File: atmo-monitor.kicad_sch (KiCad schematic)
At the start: 29 parts, among them J1 E-Ink, J3 Qwiic, J4 PM Sensor, Q1 IRLML0100TRPbF, SW1 Reset, SW2 1825232-1, U1 STM32F103CBT6, U2 LP2950-3.3_TO252, U3 Power

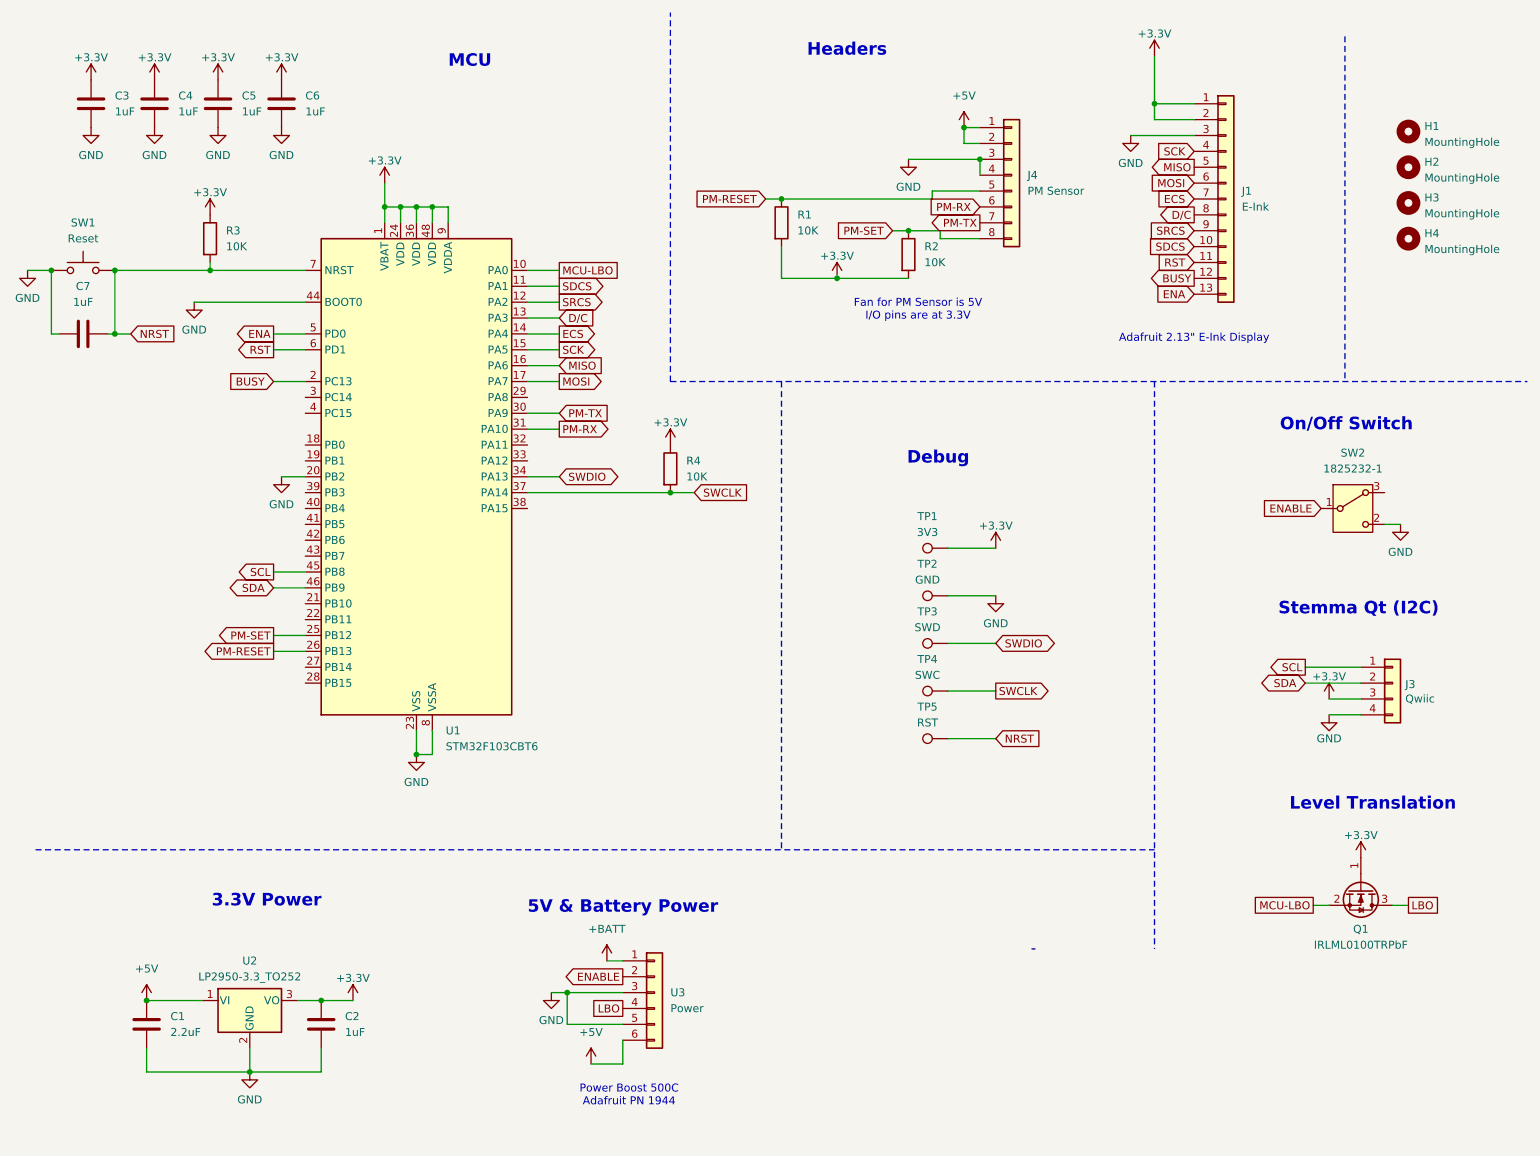
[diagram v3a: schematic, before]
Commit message: Added R5 for LBO pull up on MCU
For proper level translation, need R5
Swapped RX and TX on PMS jumper so that it is legibly correct
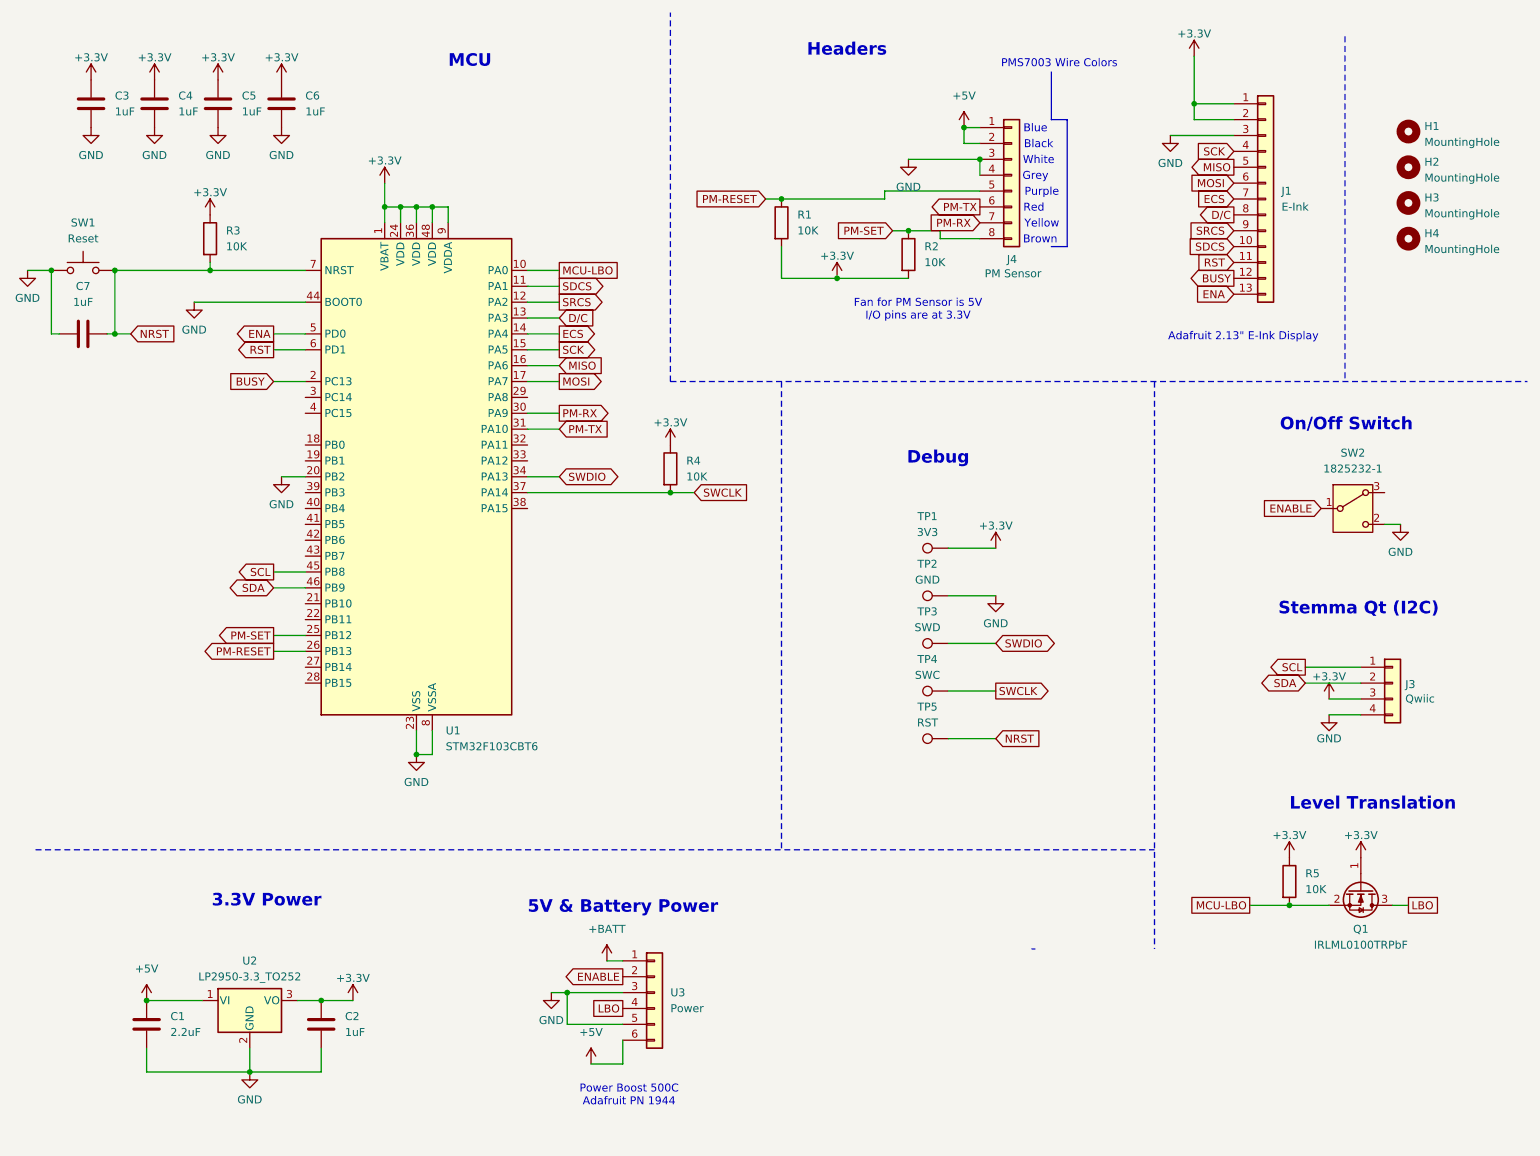
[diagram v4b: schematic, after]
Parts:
- added R5: 10K, Resistor_SMD:R_1206_3216Metric_Pad1.30x1.75mm_HandSolder, symbol Device:R
- SW1: footprint (none) -> custom_footprint:OnShine KPT-1187B
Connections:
- net +3.3V: now also R5.1
- net MCU-LBO: now also R5.2
- net PM-RX: now also J4.7 (Pin_7), U1.30 (PA9); no longer J4.6 (Pin_6), U1.31 (PA10)
- net PM-TX: now also J4.6 (Pin_6), U1.31 (PA10); no longer J4.7 (Pin_7), U1.30 (PA9)
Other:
- note added: "Black"
- note added: "Blue"
- note added: "Brown"
- note added: "Grey"
- note added: "PMS7003 Wire Colors"
- note added: "Purple"
- note added: "Red"
- note added: "White"
- note added: "Yellow"
- moved on the sheet: J1

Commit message: Finished schematic drc checks
Update pdb from schematic, no real changes
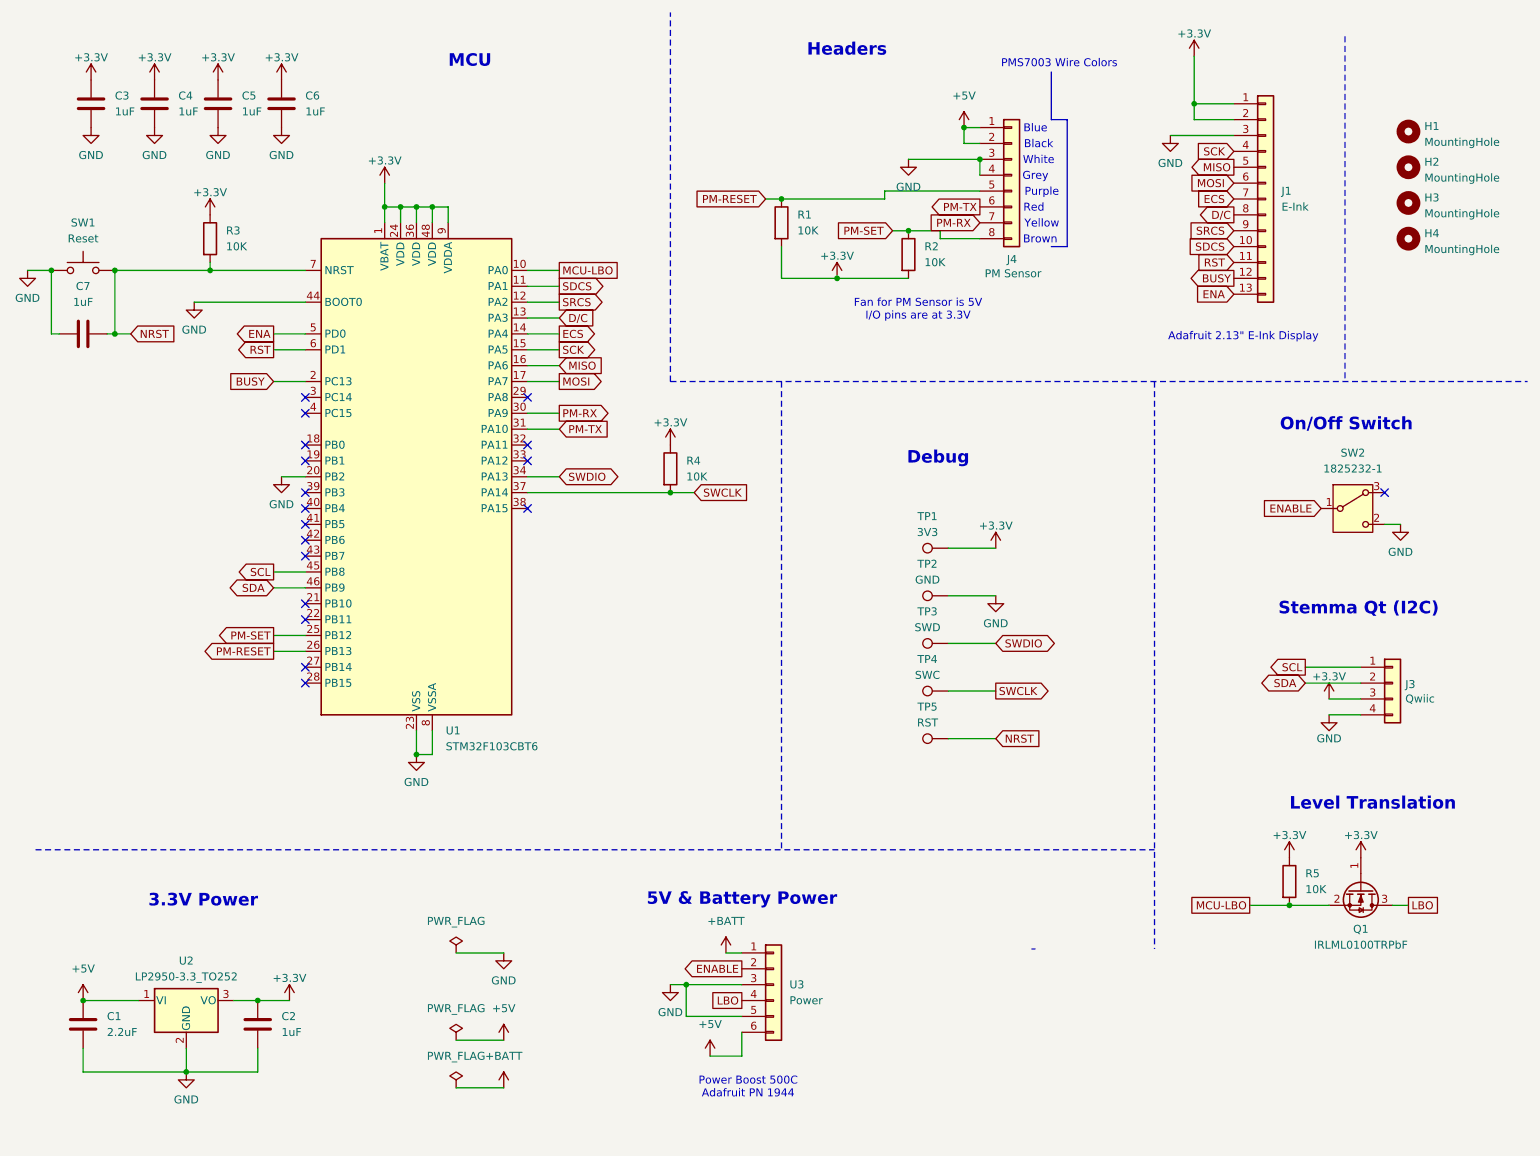
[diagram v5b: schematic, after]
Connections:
- no-connect marks 0 -> 18
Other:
- moved on the sheet: C1, C2, U2, U3
